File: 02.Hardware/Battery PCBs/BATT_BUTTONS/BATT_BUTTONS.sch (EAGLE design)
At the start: 4 parts

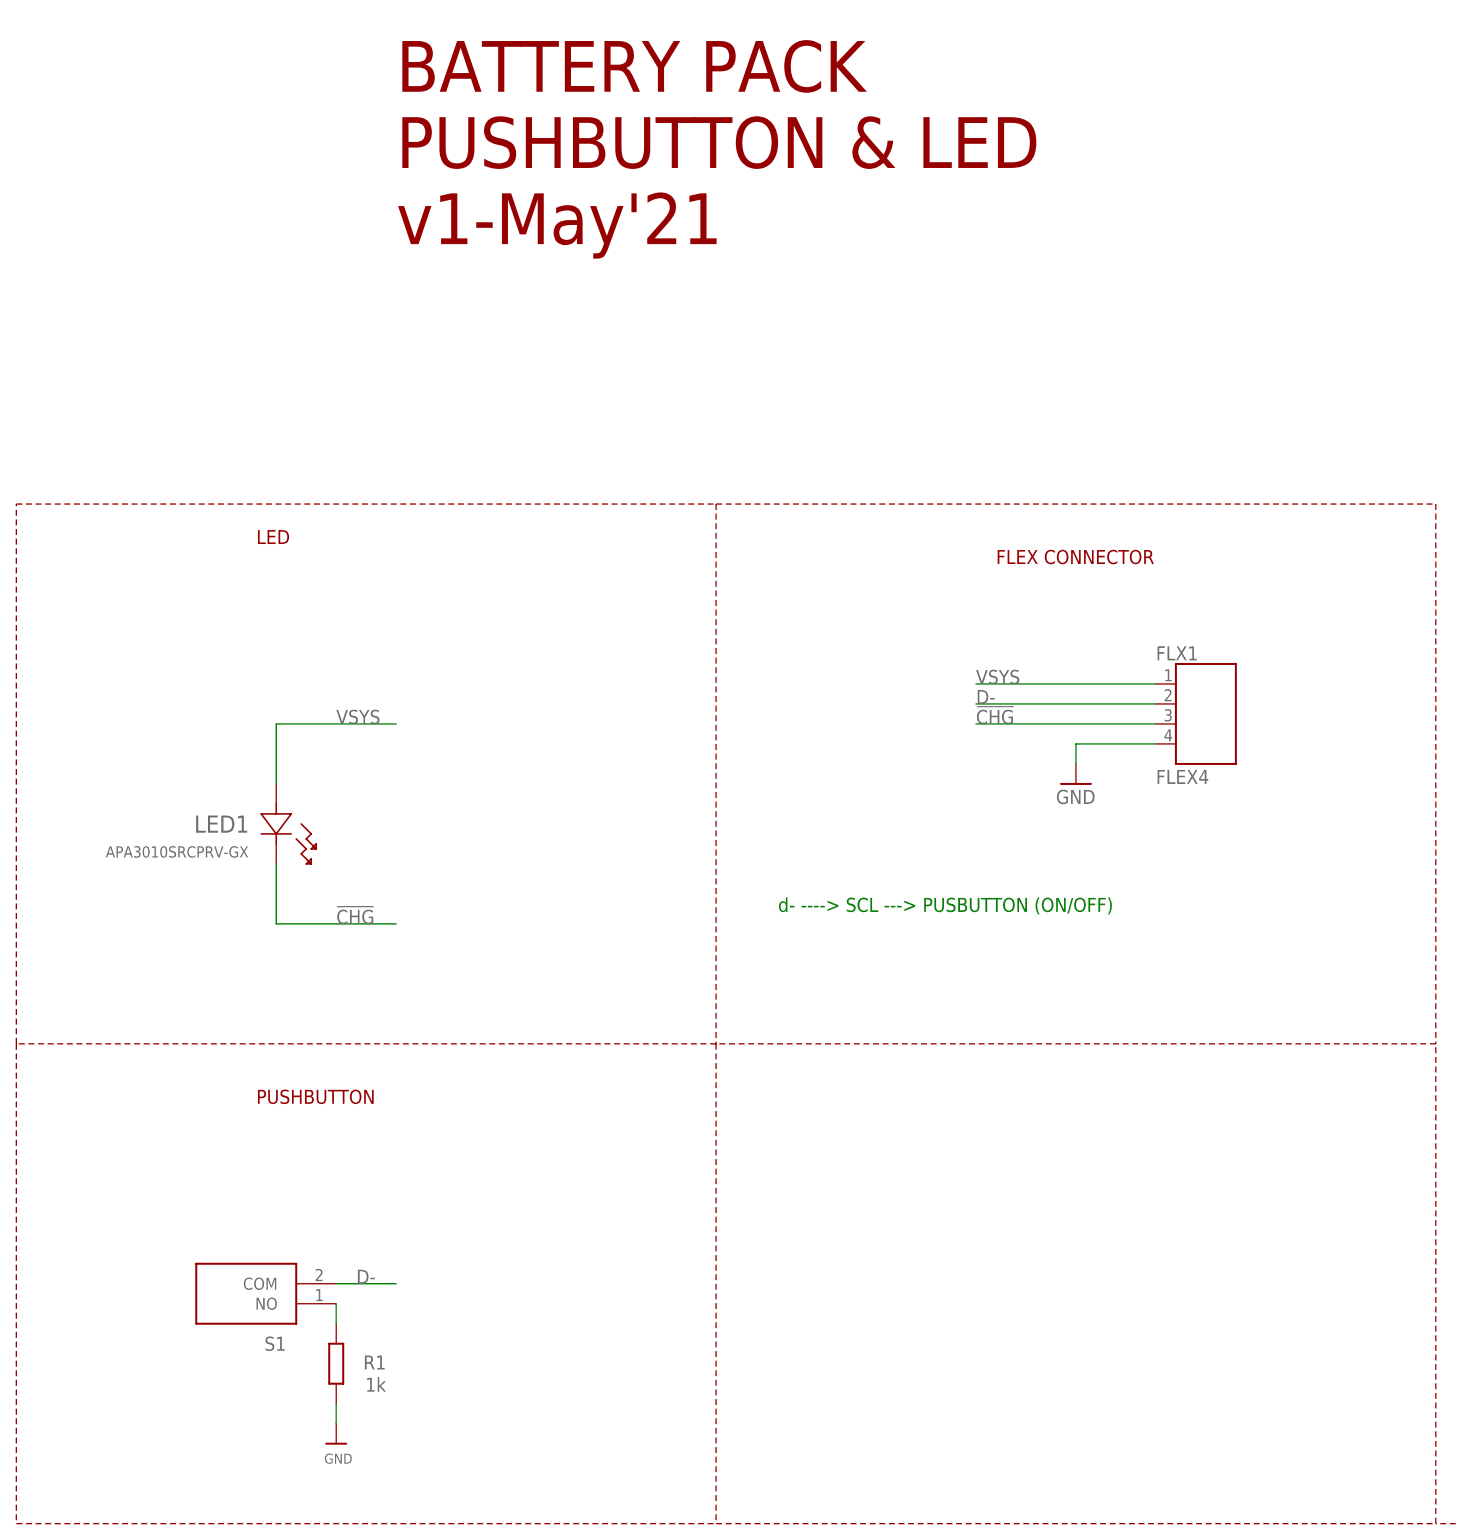
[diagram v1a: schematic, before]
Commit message: Cambios revisados con David
Revision de los pcbs de la bateria.

En el DCDC se añade un diode Clamp (bat54s) en la medicion de la tension de salida.
Actualizacion de la BOM a v8.
Documentos de Cambios de versiones
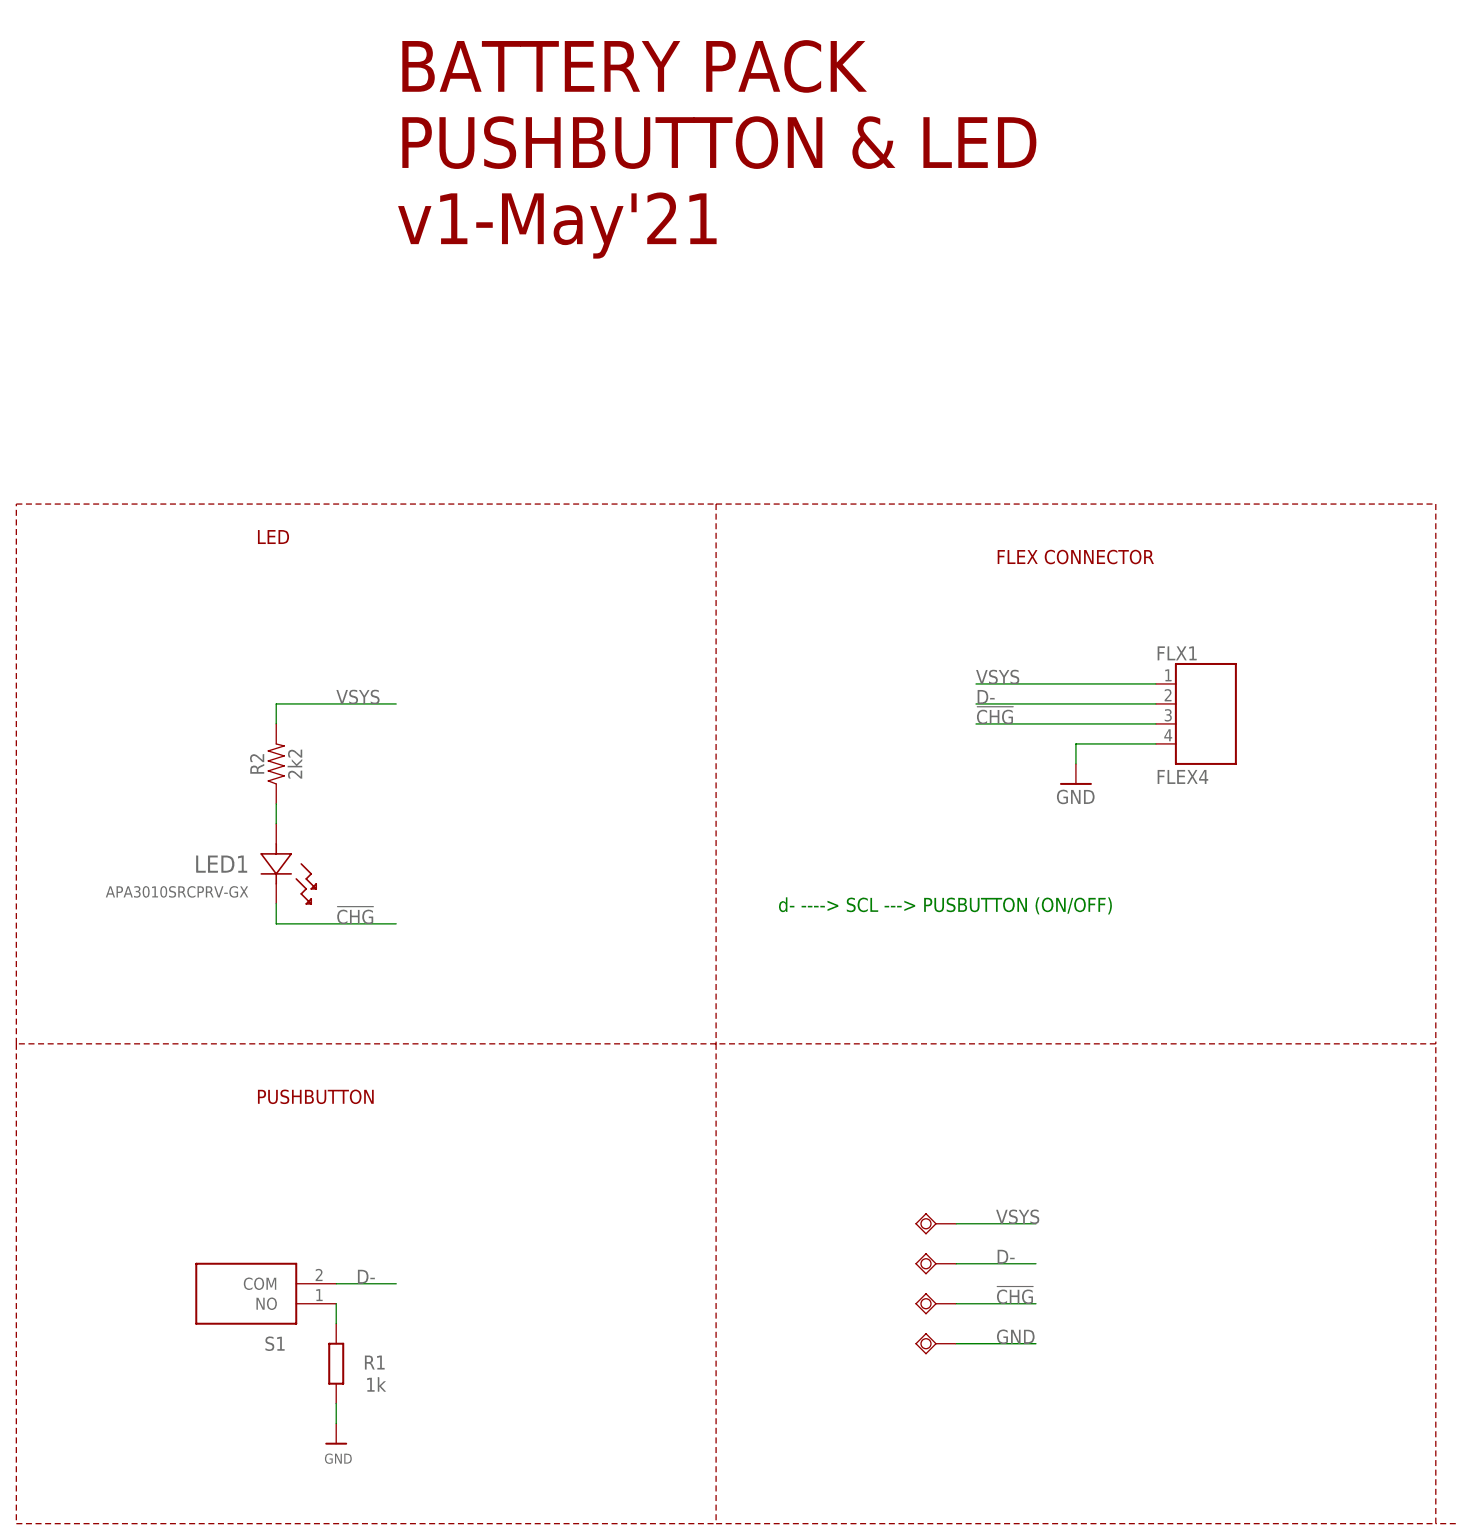
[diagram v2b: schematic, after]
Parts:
- added !CHG, D-, GND, VSYS: TESTPAD_TPSQB1,27, BeagleBone_Blue_R3:TESTPAD_TPSQB1,27
- added R2: 2k2, SparkFun-Resistors:RESISTOR0402
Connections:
- new net N$2: LED1.2, R2.1
- net !CHG!: now also !CHG.TP
- net D-: now also D-.TP
- net GND: now also GND.TP
- net VSYS: now also R2.2, VSYS.TP; no longer LED1.2
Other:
- moved on the sheet: LED1
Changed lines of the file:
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@@
 <part name="GND10" library="SparkFun-Aesthetics" deviceset="GND" device=""/>
 <part name="LED1" library="APA3010 Led" deviceset="APA3010SRCPRV-GX" device=""/>
+<part name="R2" library="SparkFun-Resistors" library_urn="urn:adsk.eagle:library:532" deviceset="RESISTOR" device="0402" package3d_urn="urn:adsk.eagle:package:39657/1" value="2k2"/>
+<part name="D-" library="BeagleBone_Blue_R3" deviceset="TESTPAD_TPSQ" device="B1,27"/>
+<part name="!CHG" library="BeagleBone_Blue_R3" deviceset="TESTPAD_TPSQ" device="B1,27"/>
+<part name="VSYS" library="BeagleBone_Blue_R3" deviceset="TESTPAD_TPSQ" device="B1,27"/>
+<part name="GND" library="BeagleBone_Blue_R3" deviceset="TESTPAD_TPSQ" device="B1,27"/>
 </parts>
 <sheets>
@@
 <attribute name="VALUE" x="172.72" y="73.66" size="1.778" layer="96"/>
 </instance>
-<instance part="LED1" gate="A" x="73.66" y="76.2" smashed="yes" rot="R270">
-<attribute name="VALUE" x="51.9938" y="66.8528" size="1.4224" layer="96" ratio="10" rot="SR0"/>
-<attribute name="NAME" x="63.2206" y="70.0024" size="2.1844" layer="95" ratio="10" rot="SR0"/>
+<instance part="LED1" gate="A" x="73.66" y="71.12" smashed="yes" rot="R270">
+<attribute name="VALUE" x="51.9938" y="61.7728" size="1.4224" layer="96" ratio="10" rot="SR0"/>
+<attribute name="NAME" x="63.2206" y="64.9224" size="2.1844" layer="95" ratio="10" rot="SR0"/>
+</instance>
+<instance part="R2" gate="G$1" x="73.66" y="78.74" smashed="yes" rot="R90">
+<attribute name="NAME" x="72.136" y="78.74" size="1.778" layer="95" font="vector" rot="R90" align="bottom-center"/>
+<attribute name="VALUE" x="75.184" y="78.74" size="1.778" layer="96" font="vector" rot="R90" align="top-center"/>
+</instance>
+<instance part="D-" gate="G$1" x="157.48" y="15.24" smashed="yes" rot="R270">
+<attribute name="TP_SIGNAL_NAME" x="156.21" y="12.7" size="1.778" layer="97" rot="R270"/>
+</instance>
+<instance part="!CHG" gate="G$1" x="157.48" y="10.16" smashed="yes" rot="R270">
+<attribute name="TP_SIGNAL_NAME" x="156.21" y="7.62" size="1.778" layer="97" rot="R270"/>
+</instance>
+<instance part="VSYS" gate="G$1" x="157.48" y="20.32" smashed="yes" rot="R270">
+<attribute name="TP_SIGNAL_NAME" x="156.21" y="17.78" size="1.778" layer="97" rot="R270"/>
+</instance>
+<instance part="GND" gate="G$1" x="157.48" y="5.08" smashed="yes" rot="R270">
+<attribute name="TP_SIGNAL_NAME" x="156.21" y="2.54" size="1.778" layer="97" rot="R270"/>
 </instance>
 </instances>
@@
 <wire x1="81.28" y1="-2.54" x2="81.28" y2="-5.08" width="0.1524" layer="91"/>
 </segment>
+<segment>
+<pinref part="GND" gate="G$1" pin="TP"/>
+<wire x1="160.02" y1="5.08" x2="170.18" y2="5.08" width="0.1524" layer="91"/>
+<label x="165.1" y="5.08" size="1.778" layer="95"/>
+</segment>
 </net>
 <net name="VSYS" class="0">
@@
 </segment>
 <segment>
-<pinref part="LED1" gate="A" pin="2"/>
-<wire x1="73.66" y1="76.2" x2="73.66" y2="83.82" width="0.1524" layer="91"/>
-<wire x1="73.66" y1="83.82" x2="88.9" y2="83.82" width="0.1524" layer="91"/>
-<label x="81.28" y="83.82" size="1.778" layer="95"/>
+<wire x1="73.66" y1="86.36" x2="88.9" y2="86.36" width="0.1524" layer="91"/>
+<label x="81.28" y="86.36" size="1.778" layer="95"/>
+<pinref part="R2" gate="G$1" pin="2"/>
+<wire x1="73.66" y1="86.36" x2="73.66" y2="83.82" width="0.1524" layer="91"/>
+</segment>
+<segment>
+<pinref part="VSYS" gate="G$1" pin="TP"/>
+<wire x1="160.02" y1="20.32" x2="170.18" y2="20.32" width="0.1524" layer="91"/>
+<label x="165.1" y="20.32" size="1.778" layer="95"/>
 </segment>
 </net>
@@
 <segment>
 <pinref part="LED1" gate="A" pin="1"/>
-<wire x1="73.66" y1="66.04" x2="73.66" y2="58.42" width="0.1524" layer="91"/>
+<wire x1="73.66" y1="60.96" x2="73.66" y2="58.42" width="0.1524" layer="91"/>
 <wire x1="73.66" y1="58.42" x2="88.9" y2="58.42" width="0.1524" layer="91"/>
 <label x="81.28" y="58.42" size="1.778" layer="95"/>
+</segment>
+<segment>
+<pinref part="!CHG" gate="G$1" pin="TP"/>
+<wire x1="160.02" y1="10.16" x2="170.18" y2="10.16" width="0.1524" layer="91"/>
+<label x="165.1" y="10.16" size="1.778" layer="95"/>
 </segment>
 </net>
@@
 <label x="83.82" y="12.7" size="1.778" layer="95"/>
 </segment>
+<segment>
+<pinref part="D-" gate="G$1" pin="TP"/>
+<wire x1="160.02" y1="15.24" x2="170.18" y2="15.24" width="0.1524" layer="91"/>
+<label x="165.1" y="15.24" size="1.778" layer="95"/>
+</segment>
 </net>
 <net name="N$1" class="0">
@@
 <pinref part="S1" gate="G$1" pin="NO"/>
 <wire x1="81.28" y1="7.62" x2="81.28" y2="10.16" width="0.1524" layer="91"/>
+</segment>
+</net>
+<net name="N$2" class="0">
+<segment>
+<pinref part="R2" gate="G$1" pin="1"/>
+<pinref part="LED1" gate="A" pin="2"/>
+<wire x1="73.66" y1="73.66" x2="73.66" y2="71.12" width="0.1524" layer="91"/>
 </segment>
 </net>
@@
 which will not be processed correctly with this version.
 </note>
+<note version="8.2" severity="warning">
+Since Version 8.2, EAGLE supports online libraries. The ids
+of those online libraries will not be understood (or retained)
+with this version.
+</note>
+<note version="8.3" severity="warning">
+Since Version 8.3, EAGLE supports URNs for individual library
+assets (packages, symbols, and devices). The URNs of those assets
+will not be understood (or retained) with this version.
+</note>
+<note version="8.3" severity="warning">
+Since Version 8.3, EAGLE supports the association of 3D packages
+with devices in libraries, schematics, and board files. Those 3D
+packages will not be understood (or retained) with this version.
+</note>
 </compatibility>

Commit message: Revision general antes de produccion
R1--> 330R (este era el valor real usado en las pruebas)
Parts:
- LED1: value APA3010SRCPRV-GX -> APA3010ZGC-GX
- R1: value 1k -> 330R
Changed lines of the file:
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@@
 <parts>
 <part name="S1" library="switch momentary CK KXT311LHS" deviceset="KXT311LHS" device=""/>
-<part name="R1" library="rcl" deviceset="R-EU_" device="R0603" value="1k"/>
+<part name="R1" library="rcl" deviceset="R-EU_" device="R0603" value="330R"/>
 <part name="U$5" library="microbuilder" deviceset="GND" device=""/>
 <part name="FLX1" library="Flex4" deviceset="FLEX4" device=""/>
 <part name="GND10" library="SparkFun-Aesthetics" deviceset="GND" device=""/>
-<part name="LED1" library="APA3010 Led" deviceset="APA3010SRCPRV-GX" device=""/>
+<part name="LED1" library="APA3010 Led" deviceset="APA3010SRCPRV-GX" device="" value="APA3010ZGC-GX"/>
 <part name="R2" library="SparkFun-Resistors" library_urn="urn:adsk.eagle:library:532" deviceset="RESISTOR" device="0402" package3d_urn="urn:adsk.eagle:package:39657/1" value="2k2"/>
 <part name="D-" library="BeagleBone_Blue_R3" deviceset="TESTPAD_TPSQ" device="B1,27"/>
